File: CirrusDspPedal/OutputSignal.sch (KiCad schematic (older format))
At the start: 9 parts, among them J2 MonoJack2Switch, U3 CS4344

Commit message: Added Footswitches and relay
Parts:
- J2: footprint (none) -> NeutrikNRJ:NRJxHx_NOTAB
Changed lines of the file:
@@
 $Descr A4 11693 8268
 encoding utf-8
-Sheet 4 8
+Sheet 4 10
 Title ""
 Date ""
@@
 F 0 "J2" H 7098 3401 50  0000 R CNN
 F 1 "MonoJack2Switch" H 7098 3310 50  0000 R CNN
-F 2 "" H 7400 3400 50  0001 C CNN
+F 2 "NeutrikNRJ:NRJxHx_NOTAB" H 7400 3400 50  0001 C CNN
 F 3 "" H 7400 3400 50  0001 C CNN
 	1    7400 3350

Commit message: updates
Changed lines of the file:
@@
 $Descr A4 11693 8268
 encoding utf-8
-Sheet 4 11
+Sheet 4 10
 Title ""
 Date ""
@@
 S 4650 1375 1525 800
 U 5F893E1B
-F0 "sheet5F893E17" 50
+F0 "PwrFilter_CS4344" 50
 F1 "PowerFiltering.sch" 50
 F2 "VDD_OUT" I L 4650 1775 50

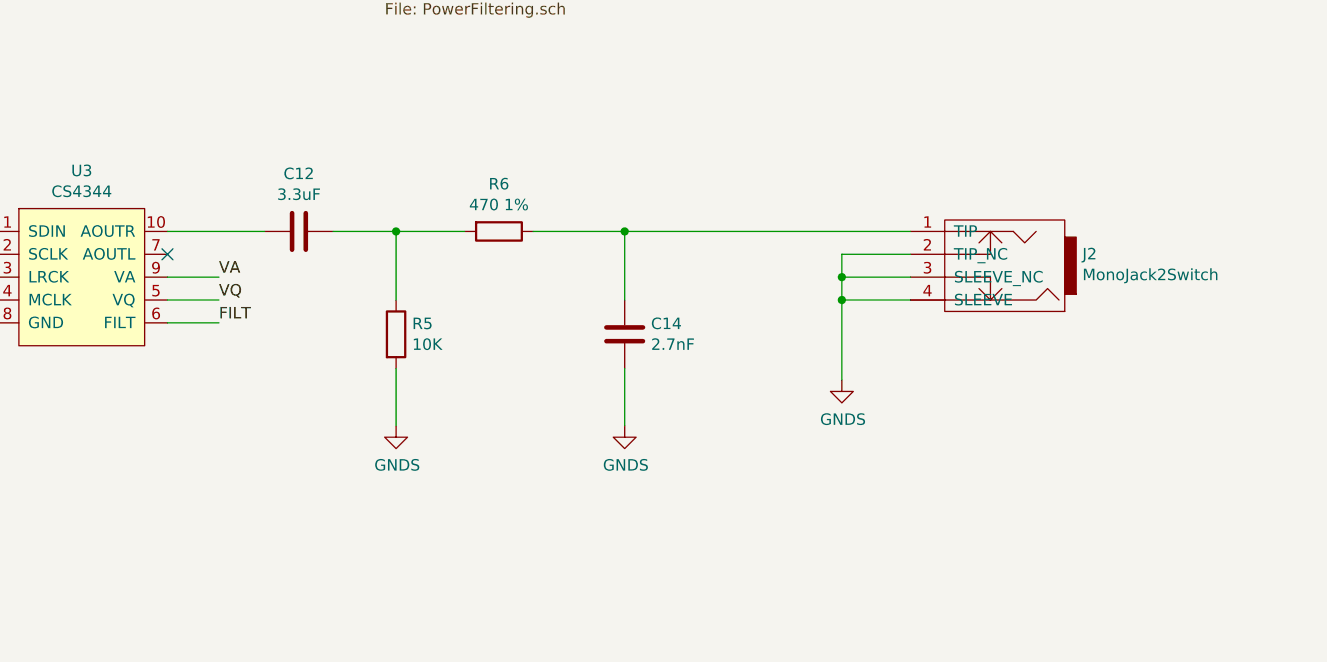
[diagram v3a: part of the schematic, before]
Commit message: Updated design
- Corrected trace going to wrong CS4344 channel output
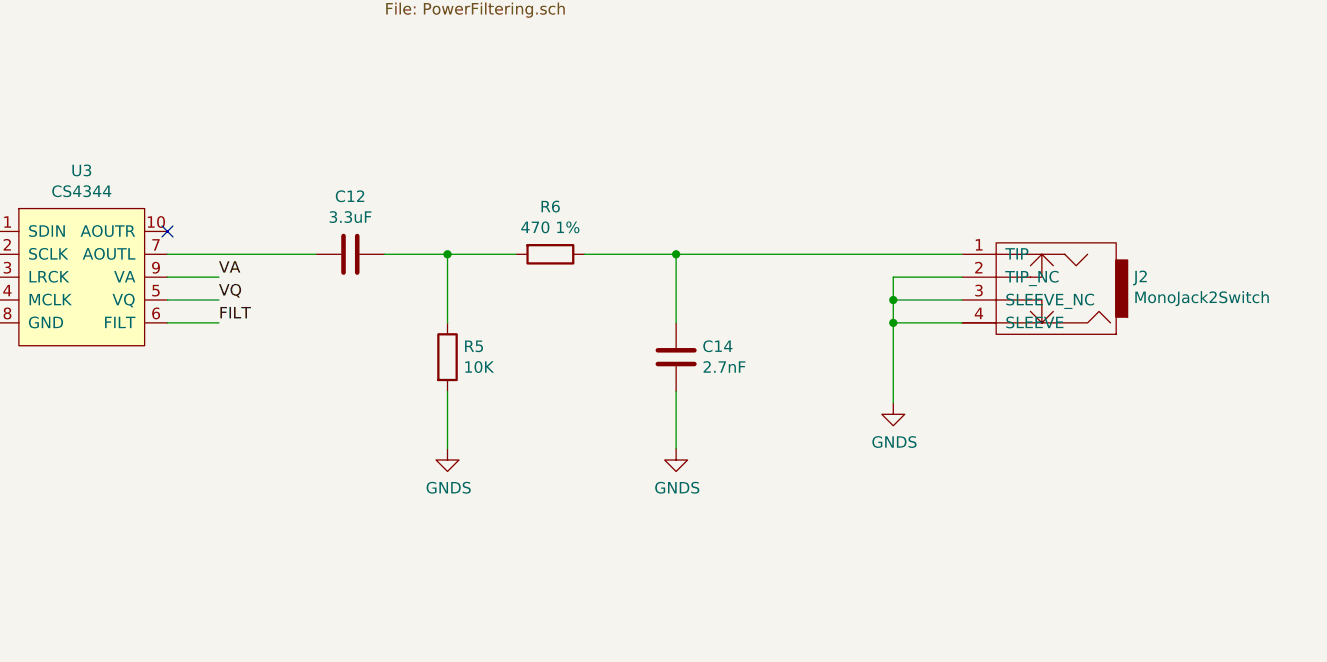
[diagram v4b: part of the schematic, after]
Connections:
- net at U3.10 (AOUTR): no longer C12.2
- net at U3.7 (AOUTL): now also C12.2
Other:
- moved on the sheet: C12, C14, J2, R5, R6
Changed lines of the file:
@@
 L MonoJack2Switch:MonoJack2Switch J?
 U 1 1 5F83CFE1
-P 7400 3350
+P 7625 3450
 AR Path="/5F83CFE1" Ref="J?"  Part="1"
 AR Path="/5F834DC7/5F83CFE1" Ref="J2"  Part="1"
-F 0 "J2" H 7098 3401 50  0000 R CNN
-F 1 "MonoJack2Switch" H 7098 3310 50  0000 R CNN
-F 2 "NeutrikNRJ:NRJxHx_NOTAB" H 7400 3400 50  0001 C CNN
-F 3 "" H 7400 3400 50  0001 C CNN
-	1    7400 3350
+F 0 "J2" H 7323 3501 50  0000 R CNN
+F 1 "MonoJack2Switch" H 7323 3410 50  0000 R CNN
+F 2 "NeutrikNRJ:NRJxHx_NOTAB" H 7625 3500 50  0001 C CNN
+F 3 "" H 7625 3500 50  0001 C CNN
+	1    7625 3450
 	-1   0    0    -1
 $EndComp
@@
 L Device:C C?
 U 1 1 5F88232C
-P 4275 3200
+P 4500 3300
 AR Path="/5F834C36/5F88232C" Ref="C?"  Part="1"
 AR Path="/5F834DC7/5F88232C" Ref="C12"  Part="1"
-F 0 "C12" V 4023 3200 50  0000 C CNN
-F 1 "3.3uF" V 4114 3200 50  0000 C CNN
-F 2 "Capacitor_SMD:C_0805_2012Metric_Pad1.15x1.40mm_HandSolder" H 4313 3050 50  0001 C CNN
-F 3 "~" H 4275 3200 50  0001 C CNN
-	1    4275 3200
+F 0 "C12" V 4248 3300 50  0000 C CNN
+F 1 "3.3uF" V 4339 3300 50  0000 C CNN
+F 2 "Capacitor_SMD:C_0805_2012Metric_Pad1.15x1.40mm_HandSolder" H 4538 3150 50  0001 C CNN
+F 3 "~" H 4500 3300 50  0001 C CNN
+	1    4500 3300
 	0    1    1    0
 $EndComp
 Wire Wire Line
-	4125 3200 3700 3200
+	4350 3300 3700 3300
 $Comp
 L Device:R R5
 U 1 1 5F8835FC
-P 4700 3650
-F 0 "R5" H 4770 3696 50  0000 L CNN
-F 1 "10K" H 4770 3605 50  0000 L CNN
-F 2 "Resistor_SMD:R_0805_2012Metric_Pad1.15x1.40mm_HandSolder" V 4630 3650 50  0001 C CNN
-F 3 "~" H 4700 3650 50  0001 C CNN
-	1    4700 3650
-	1    0    0    -1
-$EndComp
-Wire Wire Line
-	4700 3500 4700 3200
+P 4925 3750
+F 0 "R5" H 4995 3796 50  0000 L CNN
+F 1 "10K" H 4995 3705 50  0000 L CNN
+F 2 "Resistor_SMD:R_0805_2012Metric_Pad1.15x1.40mm_HandSolder" V 4855 3750 50  0001 C CNN
+F 3 "~" H 4925 3750 50  0001 C CNN
+	1    4925 3750
+	1    0    0    -1
+$EndComp
+Wire Wire Line
+	4925 3600 4925 3300
 $Comp
 L Device:R R6
 U 1 1 5F883FB6
-P 5150 3200
-F 0 "R6" V 4943 3200 50  0000 C CNN
-F 1 "470 1%" V 5034 3200 50  0000 C CNN
-F 2 "Resistor_SMD:R_0805_2012Metric_Pad1.15x1.40mm_HandSolder" V 5080 3200 50  0001 C CNN
-F 3 "~" H 5150 3200 50  0001 C CNN
-	1    5150 3200
+P 5375 3300
+F 0 "R6" V 5168 3300 50  0000 C CNN
+F 1 "470 1%" V 5259 3300 50  0000 C CNN
+F 2 "Resistor_SMD:R_0805_2012Metric_Pad1.15x1.40mm_HandSolder" V 5305 3300 50  0001 C CNN
+F 3 "~" H 5375 3300 50  0001 C CNN
+	1    5375 3300
 	0    1    1    0
 $EndComp
 Wire Wire Line
-	4425 3200 4700 3200
-Connection ~ 4700 3200
-Wire Wire Line
-	4700 3200 5000 3200
-Wire Wire Line
-	4700 3800 4700 4050
+	4650 3300 4925 3300
+Connection ~ 4925 3300
+Wire Wire Line
+	4925 3300 5225 3300
+Wire Wire Line
+	4925 3900 4925 4150
 $Comp
 L power:GNDS #PWR0113
 U 1 1 5F884D91
-P 4700 4050
-F 0 "#PWR0113" H 4700 3800 50  0001 C CNN
-F 1 "GNDS" H 4705 3877 50  0000 C CNN
-F 2 "" H 4700 4050 50  0001 C CNN
-F 3 "" H 4700 4050 50  0001 C CNN
-	1    4700 4050
+P 4925 4150
+F 0 "#PWR0113" H 4925 3900 50  0001 C CNN
+F 1 "GNDS" H 4930 3977 50  0000 C CNN
+F 2 "" H 4925 4150 50  0001 C CNN
+F 3 "" H 4925 4150 50  0001 C CNN
+	1    4925 4150
 	1    0    0    -1
 $EndComp
@@
 L Device:C C?
 U 1 1 5F884DC5
-P 5700 3650
+P 5925 3750
 AR Path="/5F834C36/5F884DC5" Ref="C?"  Part="1"
 AR Path="/5F834DC7/5F884DC5" Ref="C14"  Part="1"
-F 0 "C14" H 5585 3604 50  0000 R CNN
-F 1 "2.7nF" H 5585 3695 50  0000 R CNN
-F 2 "Capacitor_SMD:C_0805_2012Metric_Pad1.15x1.40mm_HandSolder" H 5738 3500 50  0001 C CNN
-F 3 "~" H 5700 3650 50  0001 C CNN
-	1    5700 3650
+F 0 "C14" H 5810 3704 50  0000 R CNN
+F 1 "2.7nF" H 5810 3795 50  0000 R CNN
+F 2 "Capacitor_SMD:C_0805_2012Metric_Pad1.15x1.40mm_HandSolder" H 5963 3600 50  0001 C CNN
+F 3 "~" H 5925 3750 50  0001 C CNN
+	1    5925 3750
 	-1   0    0    1
 $EndComp
 Wire Wire Line
-	5700 3500 5700 3200
-Wire Wire Line
-	5700 3200 5300 3200
-Wire Wire Line
-	5700 3800 5700 4050
+	5925 3600 5925 3300
+Wire Wire Line
+	5925 3300 5525 3300
+Wire Wire Line
+	5925 3900 5925 4150
 $Comp
 L power:GNDS #PWR0114
 U 1 1 5F886321
-P 5700 4050
-F 0 "#PWR0114" H 5700 3800 50  0001 C CNN
-F 1 "GNDS" H 5705 3877 50  0000 C CNN
-F 2 "" H 5700 4050 50  0001 C CNN
-F 3 "" H 5700 4050 50  0001 C CNN
-	1    5700 4050
+P 5925 4150
+F 0 "#PWR0114" H 5925 3900 50  0001 C CNN
+F 1 "GNDS" H 5930 3977 50  0000 C CNN
+F 2 "" H 5925 4150 50  0001 C CNN
+F 3 "" H 5925 4150 50  0001 C CNN
+	1    5925 4150
 	1    0    0    -1
 $EndComp
@@
 Text Label 3925 3400 0    50   ~ 0
 VA
-NoConn ~ 3700 3300
-Wire Wire Line
-	6950 3200 5700 3200
-Connection ~ 5700 3200
-Wire Wire Line
-	6950 3500 6650 3500
-Wire Wire Line
-	6650 3500 6650 3850
+NoConn ~ 3700 3200
+Wire Wire Line
+	7175 3300 5925 3300
+Connection ~ 5925 3300
+Wire Wire Line
+	7175 3600 6875 3600
+Wire Wire Line
+	6875 3600 6875 3950
 $Comp
 L power:GNDS #PWR0129
 U 1 1 5F95C390
-P 6650 3850
-F 0 "#PWR0129" H 6650 3600 50  0001 C CNN
-F 1 "GNDS" H 6655 3677 50  0000 C CNN
-F 2 "" H 6650 3850 50  0001 C CNN
-F 3 "" H 6650 3850 50  0001 C CNN
-	1    6650 3850
-	1    0    0    -1
-$EndComp
-Wire Wire Line
-	6650 3500 6650 3400
-Wire Wire Line
-	6650 3300 6950 3300
-Connection ~ 6650 3500
-Wire Wire Line
-	6950 3400 6650 3400
-Connection ~ 6650 3400
-Wire Wire Line
-	6650 3400 6650 3300
+P 6875 3950
+F 0 "#PWR0129" H 6875 3700 50  0001 C CNN
+F 1 "GNDS" H 6880 3777 50  0000 C CNN
+F 2 "" H 6875 3950 50  0001 C CNN
+F 3 "" H 6875 3950 50  0001 C CNN
+	1    6875 3950
+	1    0    0    -1
+$EndComp
+Wire Wire Line
+	6875 3600 6875 3500
+Wire Wire Line
+	6875 3400 7175 3400
+Connection ~ 6875 3600
+Wire Wire Line
+	7175 3500 6875 3500
+Connection ~ 6875 3500
+Wire Wire Line
+	6875 3500 6875 3400
 $EndSCHEMATC

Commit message: finished revb layout
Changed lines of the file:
@@
 Wire Wire Line
 	6750 1775 6750 1575
-$Comp
-L power:+3.3V #PWR?
-U 1 1 5F893E23
-P 6750 1575
-AR Path="/5F834C36/5F893E23" Ref="#PWR?"  Part="1"
-AR Path="/5F834DC7/5F893E23" Ref="#PWR0115"  Part="1"
-F 0 "#PWR0115" H 6750 1425 50  0001 C CNN
-F 1 "+3.3V" H 6765 1748 50  0000 C CNN
-F 2 "" H 6750 1575 50  0001 C CNN
-F 3 "" H 6750 1575 50  0001 C CNN
-	1    6750 1575
-	-1   0    0    -1
-$EndComp
 Wire Wire Line
 	4650 1775 3900 1775
@@
 Wire Wire Line
 	6875 3500 6875 3400
+$Comp
+L power:+5V #PWR0115
+U 1 1 5FA73CC2
+P 6750 1575
+F 0 "#PWR0115" H 6750 1425 50  0001 C CNN
+F 1 "+5V" H 6765 1748 50  0000 C CNN
+F 2 "" H 6750 1575 50  0001 C CNN
+F 3 "" H 6750 1575 50  0001 C CNN
+	1    6750 1575
+	1    0    0    -1
+$EndComp
 $EndSCHEMATC
